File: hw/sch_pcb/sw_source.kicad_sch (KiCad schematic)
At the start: 37 parts, among them U1 TPS631000DRLR

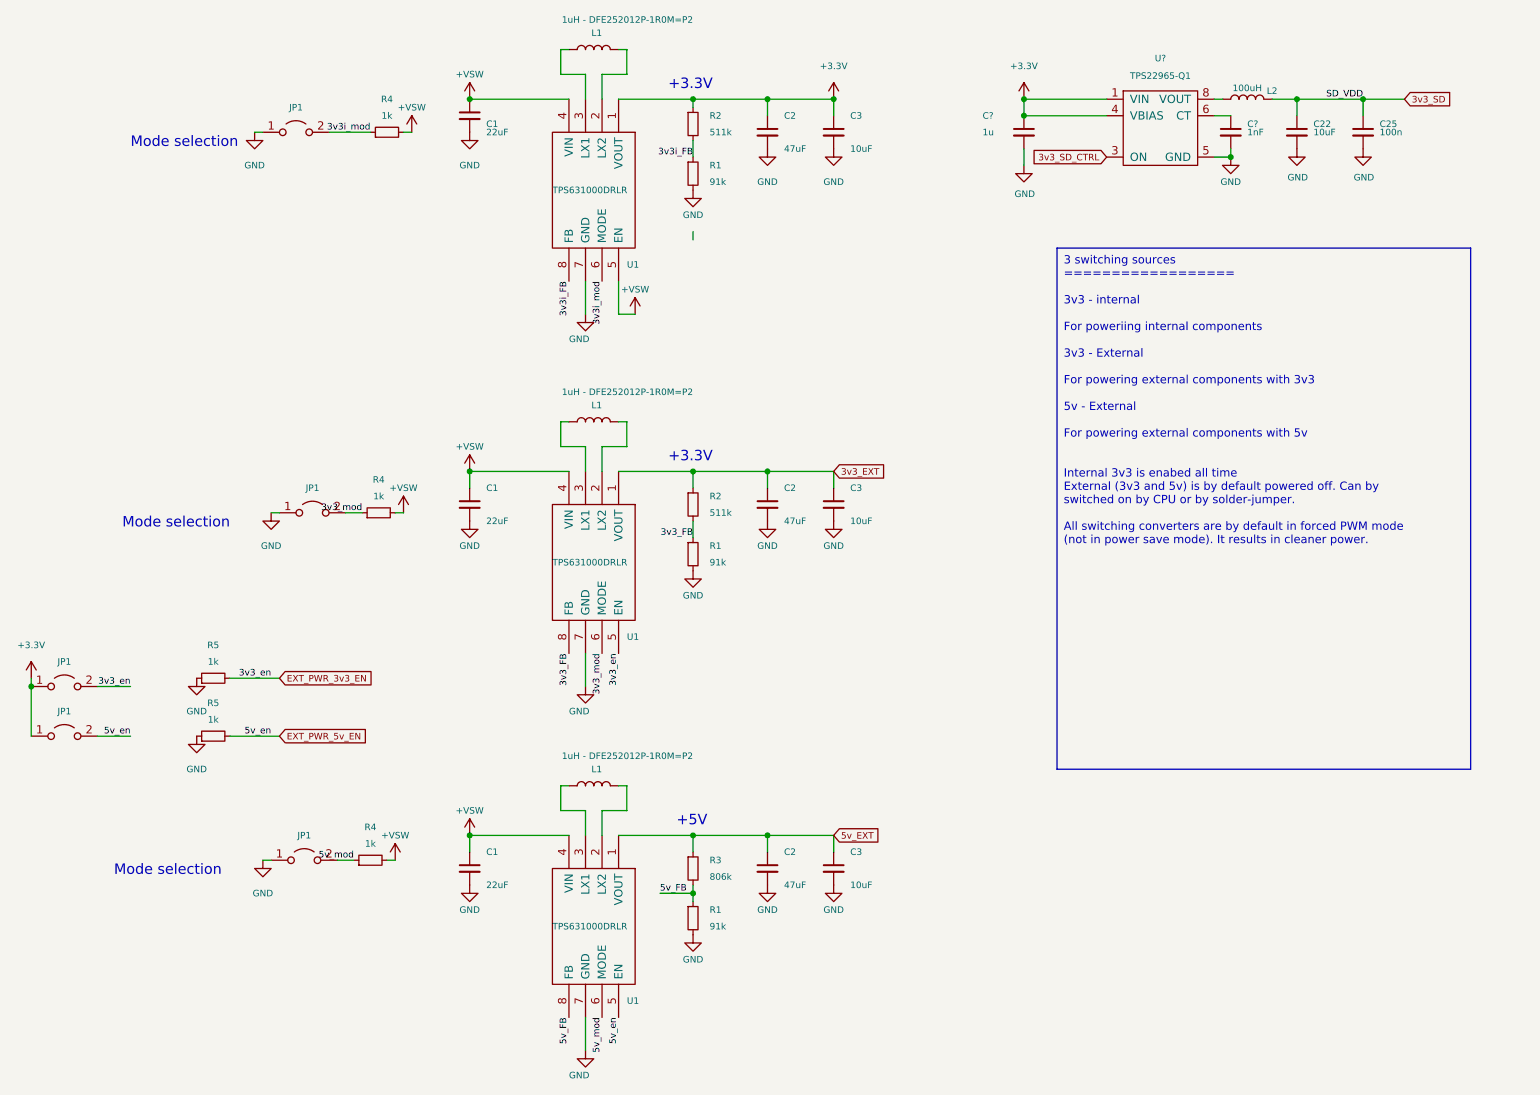
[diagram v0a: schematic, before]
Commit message: WIP, add ust ID for existing parts
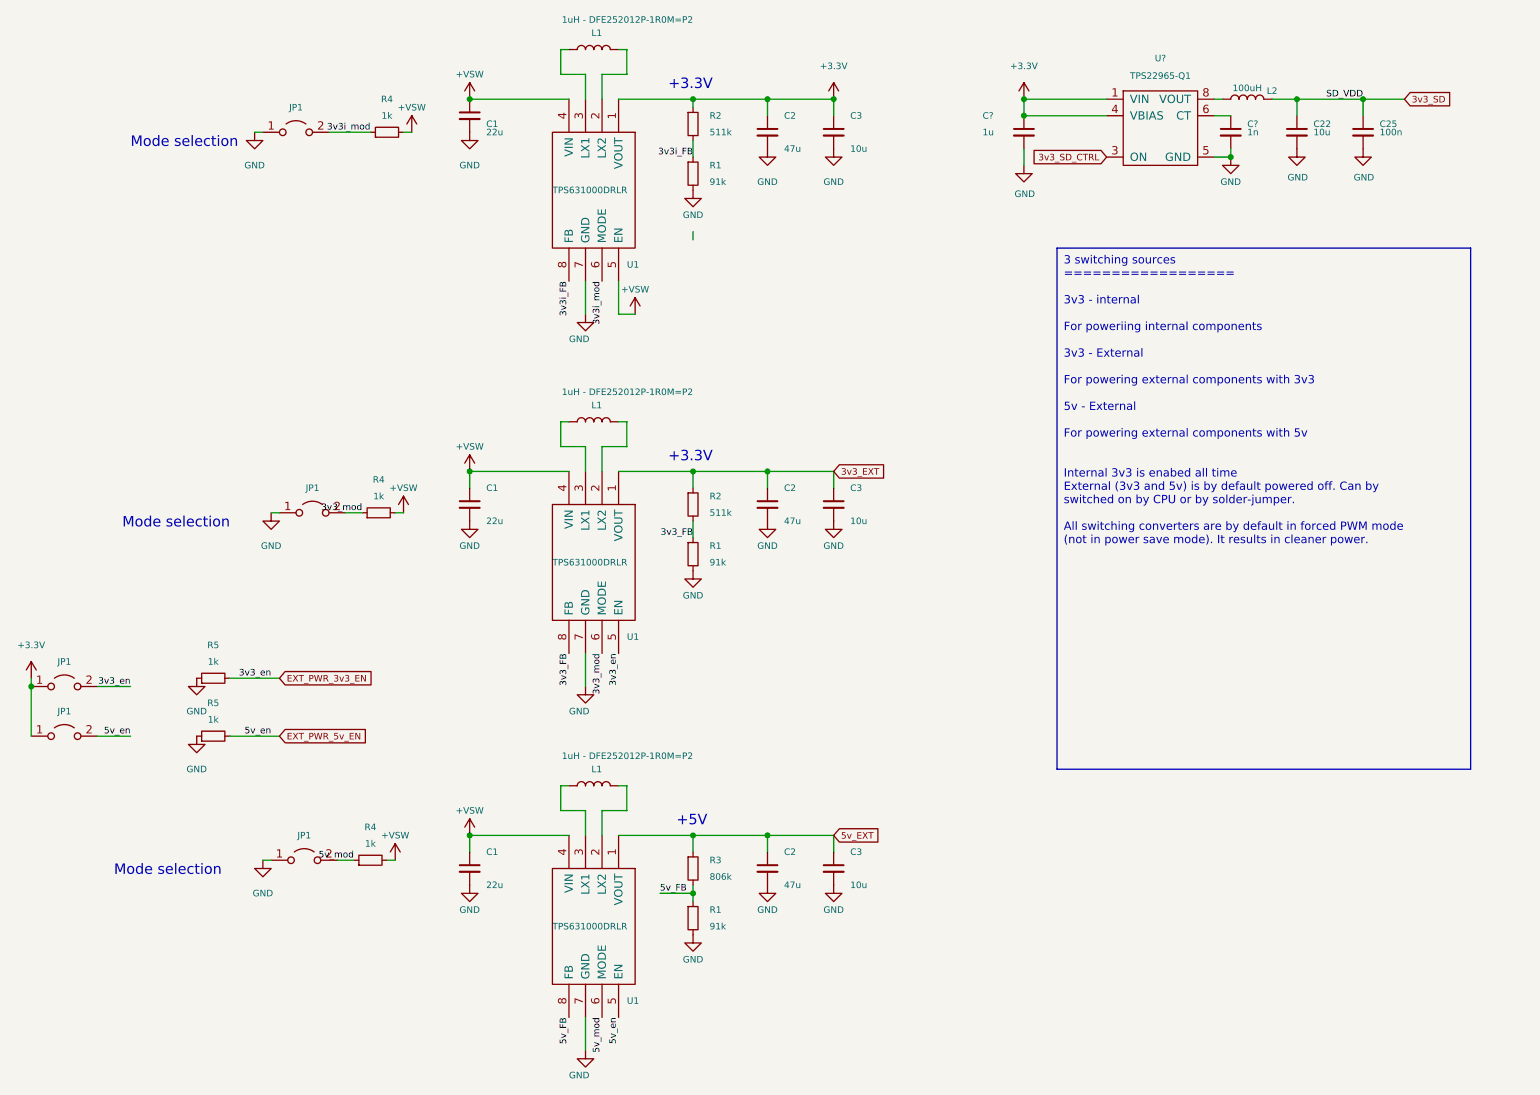
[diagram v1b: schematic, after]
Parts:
- C1: value 22uF -> 22u; UST_ID (none) -> 650b58f1462c6d9e7205463b
- C2: value 47uF -> 47u; UST_ID (none) -> 5c70984812875079b91f8bbf
- C22, C3: value 10uF -> 10u; UST_ID (none) -> 5c70984712875079b91f8b53
- C25: UST_ID (none) -> 5c70984712875079b91f8b4c
- C?: UST_ID (none) -> 5c70984712875079b91f8b50
- C?: value 1nF -> 1n; UST_ID (none) -> 5c70984712875079b91f8b45
- JP1: UST_ID (none) -> x
- L1: UST_ID (none) -> 650b5977462c6d9e72054656
- L2: UST_ID (none) -> 626fd6fcdc56076e9a222966
- R4, R5: UST_ID (none) -> 5c70984512875079b91f898c
- U?: UST_ID (none) -> 5c70984712875079b91f8b78
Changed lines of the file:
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@@
       (effects (font (size 1 1)) hide)
     )
-    (property "UST_ID" "" (at 185.42 39.37 0)
+    (property "UST_ID" "5c70984712875079b91f8b50" (at 185.42 39.37 0)
       (effects (font (size 1 1)) hide)
     )
@@
       (effects (font (size 1 1)) (justify left))
     )
-    (property "Value" "10uF" (at 158.75 41.91 0)
+    (property "Value" "10u" (at 158.75 41.91 0)
       (effects (font (size 1 1)) (justify left))
     )
@@
     (property "Datasheet" "~" (at 156.21 39.37 0)
       (effects (font (size 1 1)) hide)
+    )
+    (property "UST_ID" "5c70984712875079b91f8b53" (at 156.21 39.37 0)
+      (effects (font (size 1.27 1.27)) hide)
     )
     (pin "1")
@@
       (effects (font (size 1 1)) hide)
     )
-    (property "UST_ID" "" (at 119.38 26.67 0)
+    (property "UST_ID" "650b5977462c6d9e72054656" (at 119.38 26.67 0)
       (effects (font (size 1 1)) hide)
     )
@@
       (effects (font (size 1 1)) hide)
     )
-    (property "UST_ID" "" (at 87.63 39.37 0)
+    (property "UST_ID" "5c70984512875079b91f898c" (at 87.63 39.37 0)
       (effects (font (size 1 1)) hide)
     )
@@
       (effects (font (size 1 1)) hide)
     )
-    (property "UST_ID" "" (at 38.1 124.46 0)
+    (property "UST_ID" "x" (at 38.1 124.46 0)
       (effects (font (size 1 1)) hide)
     )
@@
       (effects (font (size 1 1)) hide)
     )
-    (property "UST_ID" "" (at 60.96 132.08 0)
+    (property "UST_ID" "5c70984512875079b91f898c" (at 60.96 132.08 0)
       (effects (font (size 1 1)) hide)
     )
@@
       (effects (font (size 1 1)) (justify left))
     )
-    (property "Value" "22uF" (at 102.87 154.94 0)
+    (property "Value" "22u" (at 102.87 154.94 0)
       (effects (font (size 1 1)) (justify left))
     )
@@
     (property "Datasheet" "~" (at 100.33 152.4 0)
       (effects (font (size 1 1)) hide)
+    )
+    (property "UST_ID" "650b58f1462c6d9e7205463b" (at 100.33 152.4 0)
+      (effects (font (size 1.27 1.27)) hide)
     )
     (pin "1")
@@
       (effects (font (size 1 1)) hide)
     )
-    (property "UST_ID" "" (at 76.2 97.79 0)
+    (property "UST_ID" "x" (at 76.2 97.79 0)
       (effects (font (size 1 1)) hide)
     )
@@
       (effects (font (size 1 1)) (justify left))
     )
-    (property "Value" "10uF" (at 158.75 99.06 0)
+    (property "Value" "10u" (at 158.75 99.06 0)
       (effects (font (size 1 1)) (justify left))
     )
@@
       (effects (font (size 1 1)) hide)
     )
+    (property "UST_ID" "5c70984712875079b91f8b53" (at 156.21 96.52 0)
+      (effects (font (size 1.27 1.27)) hide)
+    )
     (pin "1")
     (pin "2")
@@
       (effects (font (size 1 1)) (justify left))
     )
-    (property "Value" "10uF" (at 158.75 154.94 0)
+    (property "Value" "10u" (at 158.75 154.94 0)
       (effects (font (size 1 1)) (justify left))
     )
@@
       (effects (font (size 1 1)) hide)
     )
+    (property "UST_ID" "5c70984712875079b91f8b53" (at 156.21 152.4 0)
+      (effects (font (size 1.27 1.27)) hide)
+    )
     (pin "1")
     (pin "2")
@@
       (effects (font (size 1 1)) hide)
     )
-    (property "UST_ID" "" (at 60.96 123.19 0)
+    (property "UST_ID" "5c70984512875079b91f898c" (at 60.96 123.19 0)
       (effects (font (size 1 1)) hide)
     )
@@
       (effects (font (size 1 1)) (justify left))
     )
-    (property "Value" "22uF" (at 102.87 39.37 0)
+    (property "Value" "22u" (at 102.87 39.37 0)
       (effects (font (size 1 1)) (justify left))
     )
@@
     (property "Datasheet" "~" (at 100.33 36.83 0)
       (effects (font (size 1 1)) hide)
+    )
+    (property "UST_ID" "650b58f1462c6d9e7205463b" (at 100.33 36.83 0)
+      (effects (font (size 1.27 1.27)) hide)
     )
     (pin "1")
@@
       (effects (font (size 1 1)) hide)
     )
-    (property "UST_ID" "" (at 219.71 34.29 0)
+    (property "UST_ID" "626fd6fcdc56076e9a222966" (at 219.71 34.29 0)
       (effects (font (size 1 1)) hide)
     )
@@
       (effects (font (size 1 1)) (justify left))
     )
-    (property "Value" "47uF" (at 148.59 154.94 0)
+    (property "Value" "47u" (at 148.59 154.94 0)
       (effects (font (size 1 1)) (justify left))
     )
@@
       (effects (font (size 1 1)) hide)
     )
+    (property "UST_ID" "5c70984812875079b91f8bbf" (at 146.05 152.4 0)
+      (effects (font (size 1.27 1.27)) hide)
+    )
     (pin "1")
     (pin "2")
@@
       (effects (font (size 1 1)) (justify left))
     )
-    (property "Value" "22uF" (at 102.87 99.06 0)
+    (property "Value" "22u" (at 102.87 99.06 0)
       (effects (font (size 1 1)) (justify left))
     )
@@
       (effects (font (size 1 1)) hide)
     )
+    (property "UST_ID" "650b58f1462c6d9e7205463b" (at 100.33 96.52 0)
+      (effects (font (size 1.27 1.27)) hide)
+    )
     (pin "1")
     (pin "2")
@@
       (effects (font (size 1 1)) (justify left))
     )
-    (property "Value" "47uF" (at 148.59 41.91 0)
+    (property "Value" "47u" (at 148.59 41.91 0)
       (effects (font (size 1 1)) (justify left))
     )
@@
       (effects (font (size 1 1)) hide)
     )
+    (property "UST_ID" "5c70984812875079b91f8bbf" (at 146.05 39.37 0)
+      (effects (font (size 1.27 1.27)) hide)
+    )
     (pin "1")
     (pin "2")
@@
       (effects (font (size 1 1)) hide)
     )
-    (property "UST_ID" "" (at 119.38 83.82 0)
+    (property "UST_ID" "650b5977462c6d9e72054656" (at 119.38 83.82 0)
       (effects (font (size 1 1)) hide)
     )
@@
       (effects (font (size 1 1)) (justify left))
     )
-    (property "Value" "47uF" (at 148.59 99.06 0)
+    (property "Value" "47u" (at 148.59 99.06 0)
       (effects (font (size 1 1)) (justify left))
     )
@@
     (property "Datasheet" "~" (at 146.05 96.52 0)
       (effects (font (size 1 1)) hide)
+    )
+    (property "UST_ID" "5c70984812875079b91f8bbf" (at 146.05 96.52 0)
+      (effects (font (size 1.27 1.27)) hide)
     )
     (pin "1")
@@
       (effects (font (size 1 1)) hide)
     )
-    (property "UST_ID" "" (at 85.09 151.13 0)
+    (property "UST_ID" "5c70984512875079b91f898c" (at 85.09 151.13 0)
       (effects (font (size 1 1)) hide)
     )
@@
       (effects (font (size 1 1)) hide)
     )
-    (property "UST_ID" "" (at 205.74 36.83 0)
+    (property "UST_ID" "5c70984712875079b91f8b78" (at 205.74 36.83 0)
       (effects (font (size 1 1)) hide)
     )
@@
       (effects (font (size 1 1)) hide)
     )
-    (property "UST_ID" "" (at 119.38 139.7 0)
+    (property "UST_ID" "650b5977462c6d9e72054656" (at 119.38 139.7 0)
       (effects (font (size 1 1)) hide)
     )
@@
       (effects (font (size 1 1)) hide)
     )
-    (property "UST_ID" "" (at 74.93 151.13 0)
+    (property "UST_ID" "x" (at 74.93 151.13 0)
       (effects (font (size 1 1)) hide)
     )
@@
       (effects (font (size 1 1)) (justify left))
     )
-    (property "Value" "1nF" (at 219.71 39.37 0)
+    (property "Value" "1n" (at 219.71 39.37 0)
       (effects (font (size 1 1)) (justify left))
     )
@@
       (effects (font (size 1 1)) hide)
     )
-    (property "UST_ID" "" (at 217.17 39.37 0)
+    (property "UST_ID" "5c70984712875079b91f8b45" (at 217.17 39.37 0)
       (effects (font (size 1 1)) hide)
     )
@@
       (effects (font (size 1 1)) hide)
     )
-    (property "UST_ID" "" (at 73.66 39.37 0)
+    (property "UST_ID" "x" (at 73.66 39.37 0)
       (effects (font (size 1 1)) hide)
     )
@@
       (effects (font (size 1 1)) (justify left))
     )
-    (property "Value" "10uF" (at 229.87 39.37 0)
+    (property "Value" "10u" (at 229.87 39.37 0)
       (effects (font (size 1 1)) (justify left))
     )
@@
       (effects (font (size 1 1)) hide)
     )
-    (property "UST_ID" "" (at 227.33 39.37 0)
+    (property "UST_ID" "5c70984712875079b91f8b53" (at 227.33 39.37 0)
       (effects (font (size 1 1)) hide)
     )
@@
       (effects (font (size 1 1)) hide)
     )
-    (property "UST_ID" "" (at 86.36 97.79 0)
+    (property "UST_ID" "5c70984512875079b91f898c" (at 86.36 97.79 0)
       (effects (font (size 1 1)) hide)
     )
@@
       (effects (font (size 1 1)) hide)
     )
-    (property "UST_ID" "" (at 38.1 132.08 0)
+    (property "UST_ID" "x" (at 38.1 132.08 0)
       (effects (font (size 1 1)) hide)
     )
@@
       (effects (font (size 1 1)) hide)
     )
-    (property "UST_ID" "" (at 237.49 39.37 0)
-      (effects (font (size 1 1)) hide)
-    )
+    (property "UST_ID" "5c70984712875079b91f8b4c" (at 237.49 39.37 0)
+      (effects (font (size 1 1)) hide)
+    )

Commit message: WIP, schematic improvements, bigger page, reststructualized
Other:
- note removed: "Mode selection"
- moved on the sheet: C1, JP1, R4
